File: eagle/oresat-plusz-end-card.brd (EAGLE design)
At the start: 99 x 95.3 mm, 55 parts, among them J1 J-SAMTEC-TFM-110-X1-XXX-D-RA, J2 U.FL, J3 M55-7101242R, J4 M55-7101242R, J5 M55-7101242R, J6 M55-7101242R, J8 FTSH-105-XX-X-DV-K, U2 TPS63070, U3 TCAN330, U4 STM32F042K6, X2 16MHZ-2.5x2mm

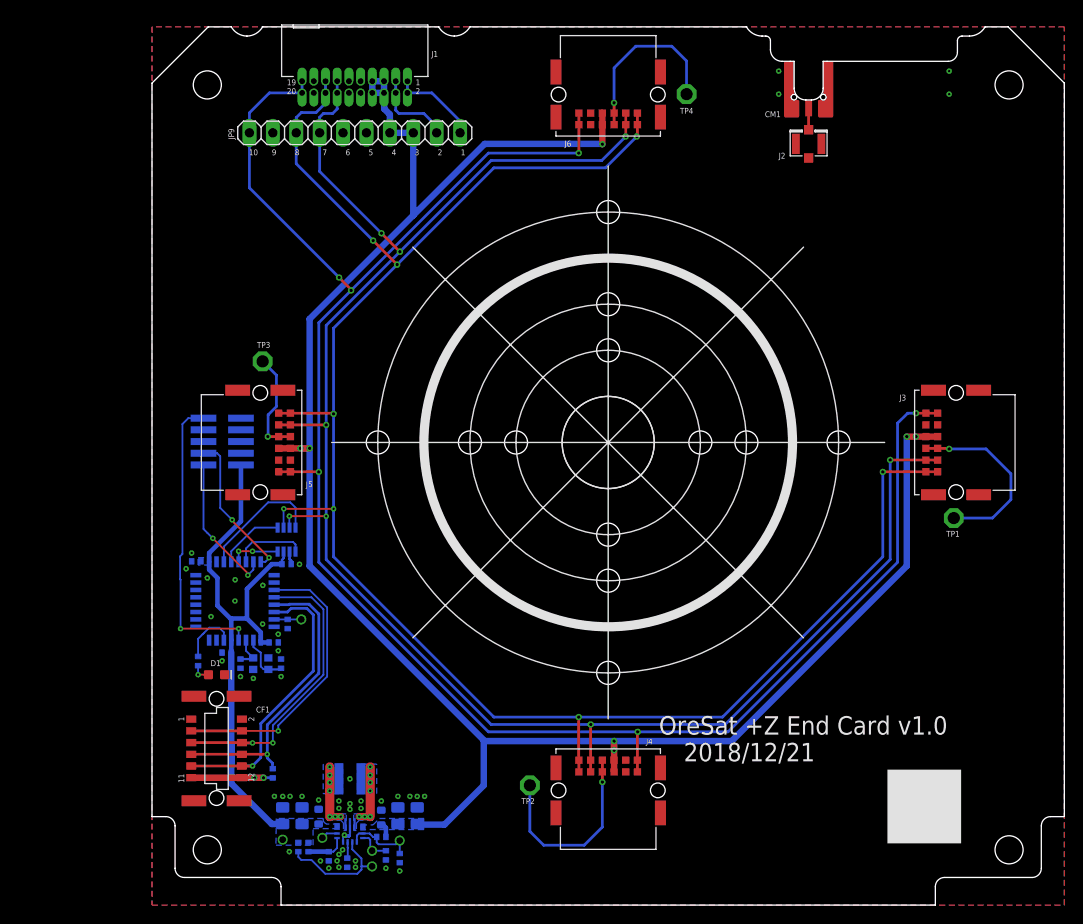
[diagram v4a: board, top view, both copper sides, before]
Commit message: Updated end cards with antenna keep outs, and rewired +Z end card debug port and started on +Z schematic update with power domain.
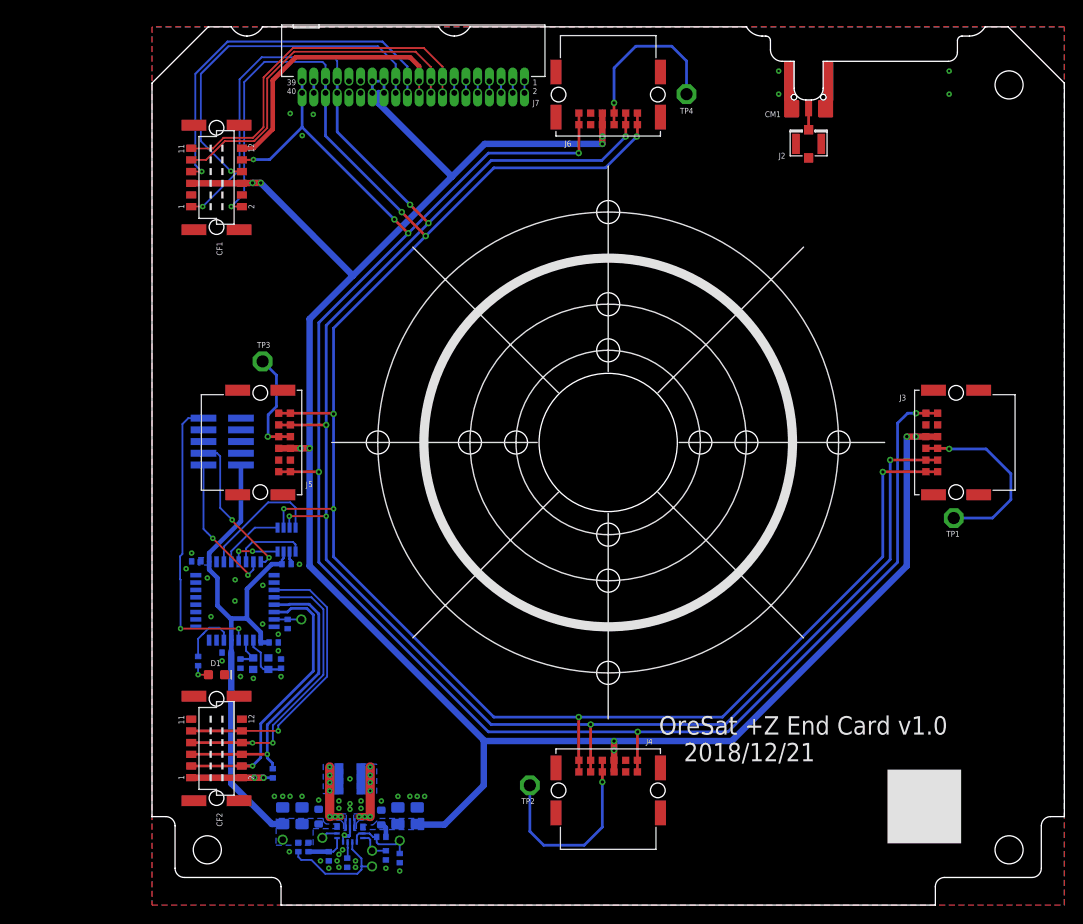
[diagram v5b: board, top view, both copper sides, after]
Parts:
- removed H3: STAND-OFFTIGHT, SparkFun-Hardware:STAND-OFF-TIGHT
- removed J1: J-SAMTEC-TFM-110-X1-XXX-D-RA, J-Samtec-TFM-110-X1-XXX-D-RA:J-SAMTEC-TFM-110-X1-XXX-D-RA
- removed JP9: (no value), pinhead:1X10
- added CF2: J-HARWIN-M55-70X1242R, J-Harwin-M55-70X1242R-12pin-1.27mm-M-vertical:HARWIN-M55-70X1242R
- added J7: J-SAMTEC-TFM-120-X1-XXX-D-RA, J-Samtec-TFM-120-X1-XXX-D-RA:J-SAMTEC-TFM-120-X1-XXX-D-RA
- CF1: value M55-7011242R -> J-HARWIN-M55-70X1242R; device J-Harwin-M55-6021242R:HARWIN-M55-6021242R -> J-Harwin-M55-70X1242R-12pin-1.27mm-M-vertical:HARWIN-M55-70X1242R
- moved CF1 62.0 mm to (7.00, 79.0)
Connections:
- new net N$15: J7.13, J7.14
- new net OPD_PWR: CF1.12, J7.19, J7.20
- new net OPD_SCL: CF1.9, J7.17, J7.18
- new net OPD_SDA: CF1.11, J7.15, J7.16
- new net SPARE1: J7.11, J7.12
- new net SPARE2: J7.10, J7.9
- new net SPARE3: J7.7, J7.8
- new net SPARE4: J7.5, J7.6
- new net SPARE5: J7.3, J7.4
- new net SPARE6: J7.1, J7.2
- net !SHUTDOWN: now also CF1.10, J7.39, J7.40; no longer J1.19, J1.20, JP9.10
- net 3.3V: now also CF2.1, CF2.2; no longer CF1.11, CF1.12
- net CAN1_H: now also CF1.1, J7.33, J7.34; no longer J1.13, J1.14, JP9.7
- net CAN1_L: now also CF1.2, J7.35, J7.36; no longer J1.15, J1.16, JP9.8
- net CAN2_H: now also CF1.7, J7.21, J7.22; no longer J1.1, J1.2, JP9.1
- net CAN2_L: now also CF1.8, J7.23, J7.24; no longer J1.3, J1.4, JP9.2
- net GND: now also CF1.3, CF1.4, CF2.11, CF2.12, CF2.P$1, CF2.P$2, CF2.P$3, CF2.P$4, J7.29, J7.30, J7.31, J7.32, J7.37, J7.38; no longer CF1.1, CF1.2, J1.10, J1.11, J1.12, J1.17, J1.18, J1.9, JP9.5, JP9.6, JP9.9
- net PB4/I2C-!RESET: now also CF2.10, CF2.9; no longer CF1.3, CF1.4
- net PB5/I2C-!INT: now also CF2.7, CF2.8; no longer CF1.5, CF1.6
- net PB6/SCL: now also CF2.5, CF2.6; no longer CF1.7, CF1.8
- net PB7/SDA: now also CF2.3, CF2.4; no longer CF1.10, CF1.9
- net VBUS: now also CF1.5, CF1.6, J7.25, J7.26, J7.27, J7.28; no longer J1.5, J1.6, J1.7, J1.8, JP9.3, JP9.4
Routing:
- net OPD_SDA: track 0.00 -> 38.6 mm
- net OPD_SCL: track 0.00 -> 37.5 mm
- net CAN2_H: track 9.52 -> 40.5 mm, vias 0 -> 1
- net CAN2_L: track 9.03 -> 39.5 mm, vias 0 -> 1
- net OPD_PWR: track 0.00 -> 29.7 mm
- net CAN1_H: track 200.0 -> 226.7 mm, vias 8 -> 9
- net CAN1_L: track 204.2 -> 225.7 mm, vias 8 -> 9
- net VBUS: track 213.2 -> 232.8 mm, vias 7 -> 10
- net !SHUTDOWN: track 204.6 -> 202.2 mm, vias 6 -> 7
- net SPARE6: track 0.00 -> 1.27 mm
- net SPARE5: track 0.00 -> 1.27 mm
- net SPARE4: track 0.00 -> 1.27 mm
- net SPARE3: track 0.00 -> 1.27 mm
- net SPARE2: track 0.00 -> 1.27 mm
- net SPARE1: track 0.00 -> 1.27 mm
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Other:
- board text removed: "1"
- board text removed: "10"
- board text removed: "2"
- board text removed: "3"
- board text removed: "4"
- board text removed: "5"
- board text removed: "6"
- board text removed: "7"
- board text removed: "8"
- board text removed: "9"

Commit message: Added OreSat power domain -- via design blocksgit status -- and OMG it's doneish.
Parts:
- removed C1: 10u, oresat-rcl:.0603-B-NOSILK
- removed C10: 22u, oresat-rcl:.0805-B-NOSILK
- removed C2: 100n, rcl_custom:.0402-B-NOSILK
- removed C3, C7: 10u, oresat-rcl:.0805-B-NOSILK
- removed R1, R4: 10k, rcl_custom:.0402-B-NOSILK
- removed R2: 470k, rcl_custom:.0402-B-NOSILK
- removed R3: 150k, rcl_custom:.0402-B-NOSILK
- removed R5, R6: NP, rcl_custom:.0402-B-NOSILK
- removed TP11, TP12, TP13, TP14, TP15: TEST-POINT, Tova:2MM-TEST-POINT
- removed U2: TPS63070, ic-pwr-tps63070x:TPS63070X
- added C16, C19, C20: 1u, oresat-rcl:.0603-B-NOSILK
- added C17: 22u, oresat-rcl:.0805-B-NOSILK
- added C6: 100n, rcl_custom:.0402-B-NOSILK
- added D5, D6: GREEN, SparkFun-LED:LED-0603
- added D7: AMBER, SparkFun-LED:LED-0603
- added Q1, Q2: MOSFET-PCH-SOT23-6, Q-MOSFET-PCH-SOT23-6:SOT23-6
- added Q7, Q8: PMV45EN, Tova:SOT23
- added R39, R40, R71: 2.7k, rcl_custom:.0402-B-NOSILK
- added R41, R54, R55: 100, rcl_custom:.0402-B-NOSILK
- added R42, R43, R44, R45, R46, R47, R48, R49, R50, R51, R52, R53, R62, R64, R66, R67, R70: NP, rcl_custom:.0402-B-NOSILK
- added R56, R57, R58, R60, R65, R68, R69: 10k, rcl_custom:.0402-B-NOSILK
- added R59: 100m, rcl:R1206
- added R61, R63: 0, rcl_custom:.0402-B-NOSILK
- added TP24, TP25, TP26, TP27, TP28, TP29, TP30, TP31, TP32, TP33, TP34, TP35, TP36, TP37, TP38, TP39, TP40, TP41: TEST-POINT, Tova:2MM-TEST-POINT
- added U10: MCP1703A, v-reg:SOT23
- added U6: MAX7310ATE, U-Maxim-MAX7310-I2C-GPIO-expander:QFN65P400X400X80-17T210
- added U8: MAX4211CETE, U-Maxim-MAX4211-power-monitor:QFN65P400X400X80-17T210
- added U9: TPS62111RSA, U-TI-TPS6211x-SPS-buck:S-PVQFN-16
- C11: value 22u -> 10u
- C9: value 22u -> NP; device oresat-rcl:.0603-B-NOSILK -> rcl_custom:.0402-B-NOSILK
- L1: value 1.5 uH -> 6.8u; device L-Coilcraft-XFL4020:L-COILCRAFT-XFL4020 -> L-ECS-MPI4040:ECS-MPI4040
- moved J8 43.6 mm to (11.6, 6.88), flipped to the top, turned to 0 degrees
- moved C9 26.3 mm to (3.10, 31.2), turned to 270 degrees
- moved C13 24.7 mm to (22.7, 5.30)
- moved C14 24.7 mm to (27.1, 5.30)
- moved C15 24.7 mm to (27.7, 16.1)
- moved C18 24.7 mm to (21.2, 6.50)
- moved C8 24.7 mm to (26.3, 7.60)
- moved R8 24.7 mm to (27.8, 9.60)
- moved R9 24.7 mm to (18.1, 5.58)
- moved TP7 24.7 mm to (29.3, 10.1)
- moved U4 24.7 mm to (22.1, 12.1)
- moved C12 24.7 mm to (17.9, 16.4)
- moved U3 24.7 mm to (27.7, 18.8)
- moved X2 24.7 mm to (24.9, 5.30)
- moved D1 21.7 mm to (18.1, 6.30), turned to 90 degrees
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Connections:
- removed net TPS-EN2: R1.1, R6.2, TP15.1, U2.1, U2.14
- removed net TPS-FB2: R2.1, R3.2, U2.5
- removed net TPS-FB4: TP13.1, U2.6
- removed net TPS-L1: L1.1, U2.11
- removed net TPS-L2: L1.2, U2.9
- removed net TPS-PG2: R5.1, TP12.1, U2.2
- removed net TPS-VAUX2: C2.1, U2.3
- removed net TPS-VSEL2: R4.2, TP14.1, U2.15
- new net !FAULT: Q8.3, R68.1, TP29.1, U6.7
- new net AD0: R42.1, R43.2, R44.2, R45.1, U6.1
- new net AD1: R46.1, R47.2, R48.2, R49.1, U6.2
- new net AD2: R50.1, R51.2, R52.2, R53.1, U6.3
- new net CB-RESET: R60.2, TP28.1, U6.5, U8.9
- new net CB_CTRL: Q1.3, Q8.1, R65.1, U8.3, U8.4, U8.6
- new net MAX4211-3V3: C20.1, U10.2, U8.1
- new net N$10: Q2.3, Q7.3, R57.1
- new net N$11: Q2.1, Q2.2, Q2.5, Q2.6, R59.1, U8.16
- new net N$12: R61.1, R62.2, TP26.1, U8.11
- new net N$13: R63.1, R64.2, TP25.1, U8.10
- new net N$14: R61.2, U8.14
- new net N$16: R63.2, U8.12, U8.8
- new net N$17: TP24.1, U8.13
- new net N$18: R67.1, U8.5
- new net N$19: C9.1, R66.2, R67.2
- new net N$20: C19.1, Q1.4, R59.2, R65.2, U10.3, U8.15
- new net N$21: TP35.1, U6.8
- new net N$22: TP36.1, U6.9
- new net N$23: TP37.1, U6.10
- new net N$24: TP38.1, U6.11
- new net N$25: R71.2, TP39.1, U6.12
- new net N$26: D7.A, R71.1
- new net N$6: D5.A, R39.1
- new net N$8: D6.A, R40.1
- new net N$9: R56.1, U6.13
- new net ON/!OFF: Q7.1, R58.2, TP27.1, U6.4
- new net PEN-SCL-FILT: R43.1, R47.1, R51.1, R54.2, TP40.1, U6.15
- new net PEN-SDA-FILT: R45.2, R49.2, R53.2, R55.2, TP41.1, U6.16
- new net TPS62111-PG1: TP31.1, U9.13
- new net TPS62111-SYNC1: R69.1, R70.2, TP32.1, U9.5
- new net TPS62111_SW1: L1.1, U9.14, U9.15
- new net VBUSP: C11.1, C16.1, C9.2, Q1.1, Q1.2, Q1.5, Q1.6, R39.2, R69.2, TP30.1, U9.2, U9.3, U9.4, U9.8
- new net VPD: C6.2, R41.2, R42.2, R46.2, R50.2, R56.2, R68.2, TP34.1, U6.14
- net 3.3V: now also C17.1, L1.2, R40.2, TP33.1, U9.10; no longer C10.1, C11.1, C9.1, R2.2, R5.2, TP11.1, U2.7-8
- net GND: now also C16.2, C17.2, C19.2, C20.2, C6.1, D5.C, D6.C, D7.C, Q7.2, Q8.2, R44.1, R48.1, R52.1, R58.1, R60.1, R62.1, R64.1, R66.1, R70.1, U10.1, U6.6, U6.EPAD, U8.7, U8.EPAD, U9.1, U9.11, U9.12, U9.16, U9.6, U9.7, U9.9, U9.PAD; no longer C1.2, C10.2, C2.2, C3.2, C7.2, C9.2, R3.1, R4.1, R6.1, U2.10, U2.4
- net OPD_PWR: now also R41.1
- net OPD_SCL: now also R54.1
- net OPD_SDA: now also R55.1
- net VBUS: now also Q2.4, R57.2; no longer C1.1, C3.1, C7.1, R1.2, U2.12-13
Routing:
- net CB_CTRL: track 0.00 -> 43.3 mm, vias 0 -> 3
- net VPD: track 0.00 -> 31.6 mm, vias 0 -> 4
- net CB-RESET: track 0.00 -> 30.5 mm, vias 0 -> 2
- net PEN-SCL-FILT: track 0.00 -> 22.9 mm, vias 0 -> 1
- net ON/!OFF: track 0.00 -> 22.6 mm
- net N$20: track 0.00 -> 18.6 mm, vias 0 -> 2
- net OPD_SDA: track 38.6 -> 57.2 mm, vias 0 -> 1
- net PEN-SDA-FILT: track 0.00 -> 18.5 mm, vias 0 -> 3
- net OPD_PWR: track 29.7 -> 47.7 mm, vias 0 -> 1
- net OPD_SCL: track 37.5 -> 52.5 mm, vias 0 -> 1
- net NRESET: track 32.4 -> 17.5 mm, vias 2 -> 1
- net VBUS: track 232.8 -> 219.2 mm
- net TPS-PG2: track 12.9 -> 0.00 mm
- net GND: track 6.00 -> 18.6 mm, vias 51 -> 63
- net VBUSP: track 0.00 -> 9.62 mm, vias 0 -> 1
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- added copper zone on layer 16, net N$11
- added copper zone on layer 16, net N$20
- added copper zone on layer 16, net TPS62111_SW1
- added copper zone on layer 16, net VBUSP
- removed copper zone on layer 16, net TPS-L1
- removed copper zone on layer 16, net TPS-L2
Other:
- board text added: "VBUSP"
- board text removed: "Vin"
